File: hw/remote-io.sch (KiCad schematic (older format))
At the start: 0 parts

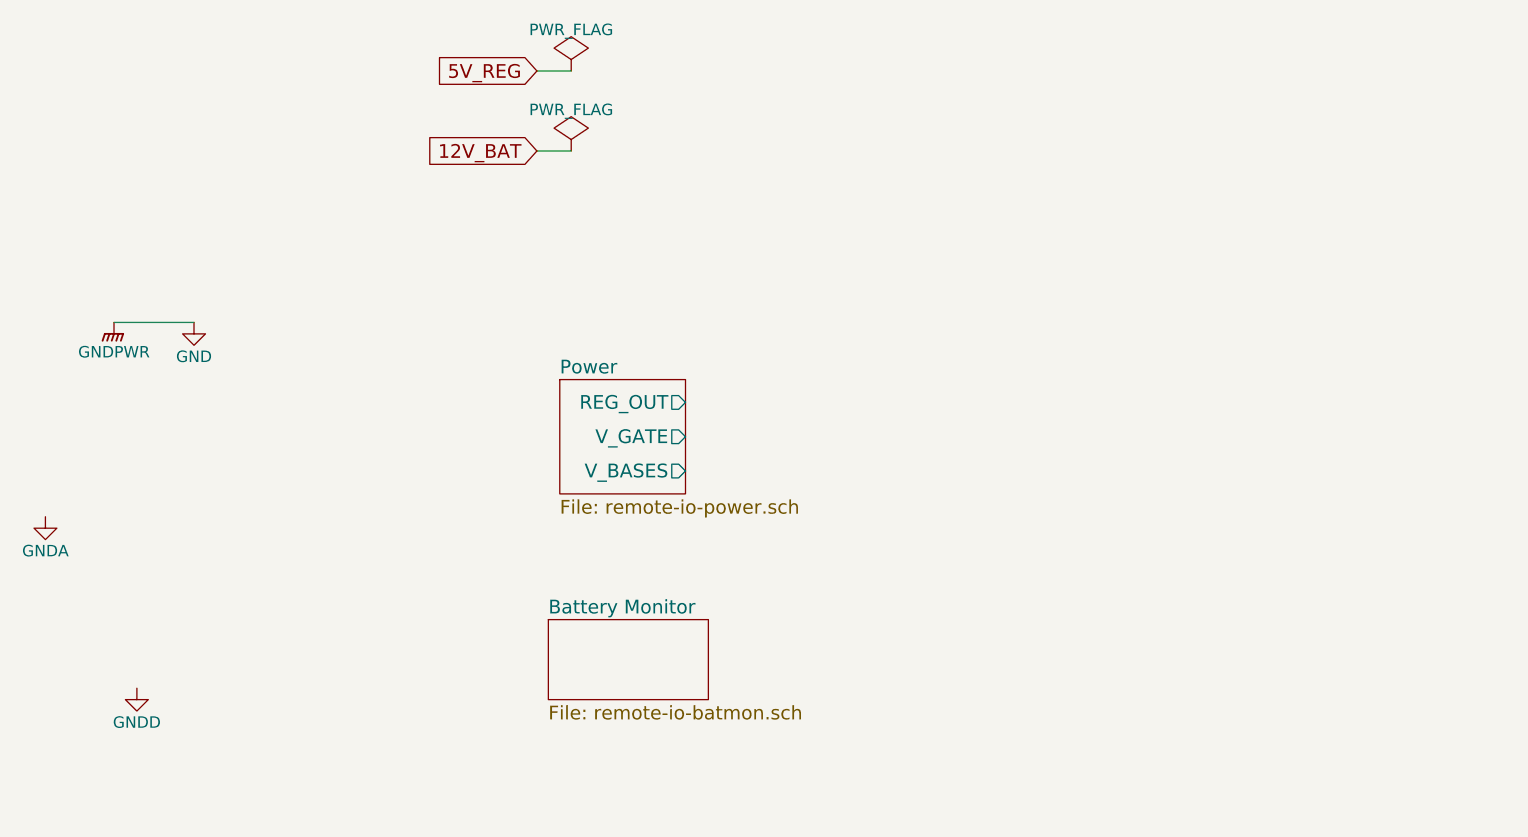
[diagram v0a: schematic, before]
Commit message: Added ADC schematic and connections
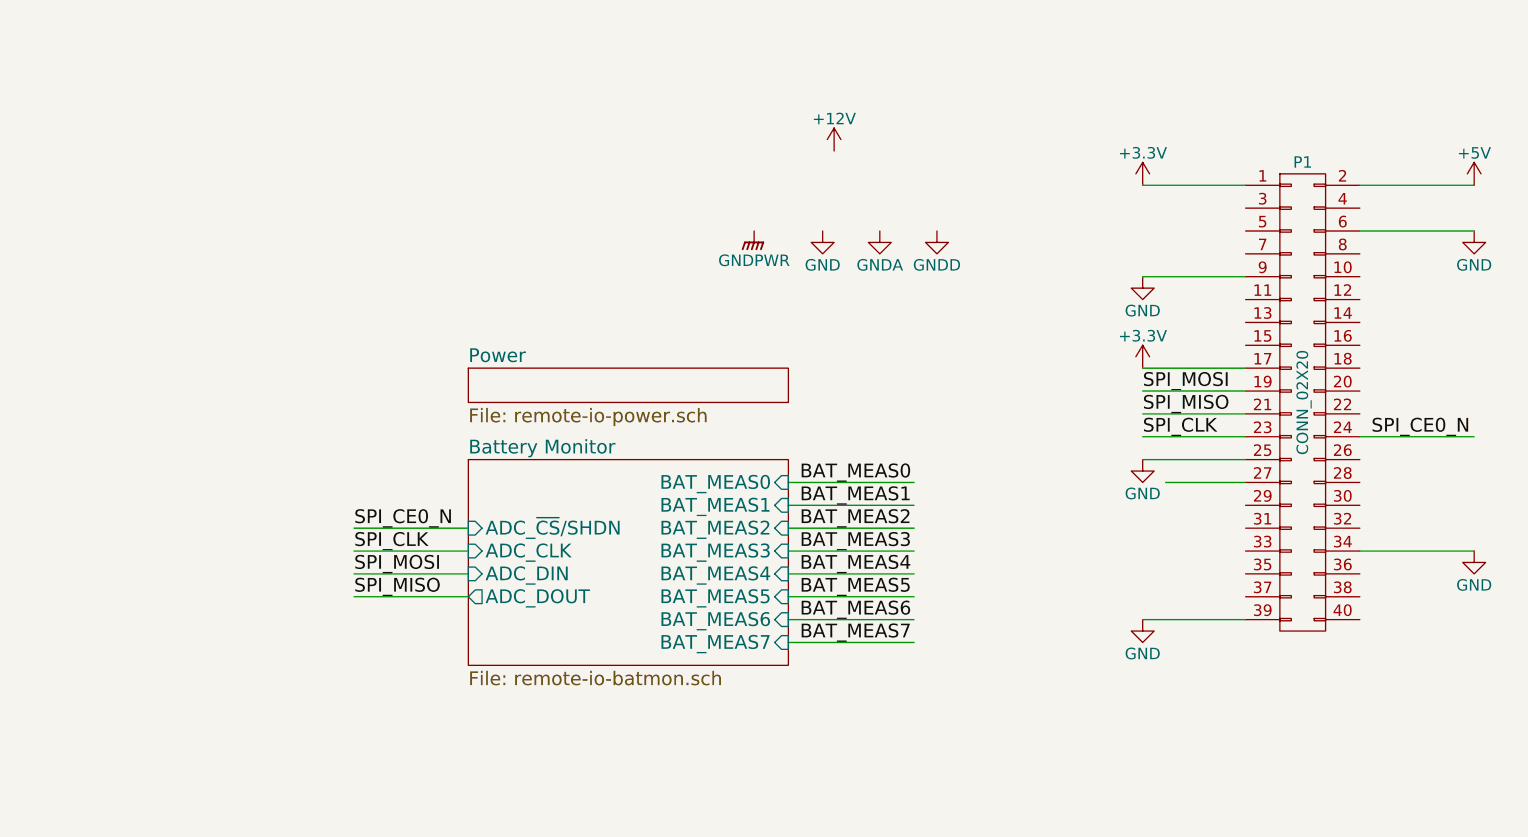
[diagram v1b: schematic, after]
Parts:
- added P1: CONN_02X20, symbol CONN_02X20
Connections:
- net labels added: +12V, +3.3V, +5V, BAT_MEAS0, BAT_MEAS1, BAT_MEAS2, BAT_MEAS3, BAT_MEAS4, BAT_MEAS5, BAT_MEAS6, BAT_MEAS7, SPI_CE0_N, SPI_CLK, SPI_MISO, SPI_MOSI
- net labels removed: 12V_BAT, 5V_REG
- wire segments 3 -> 25

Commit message: Added I2C ID EEPROM
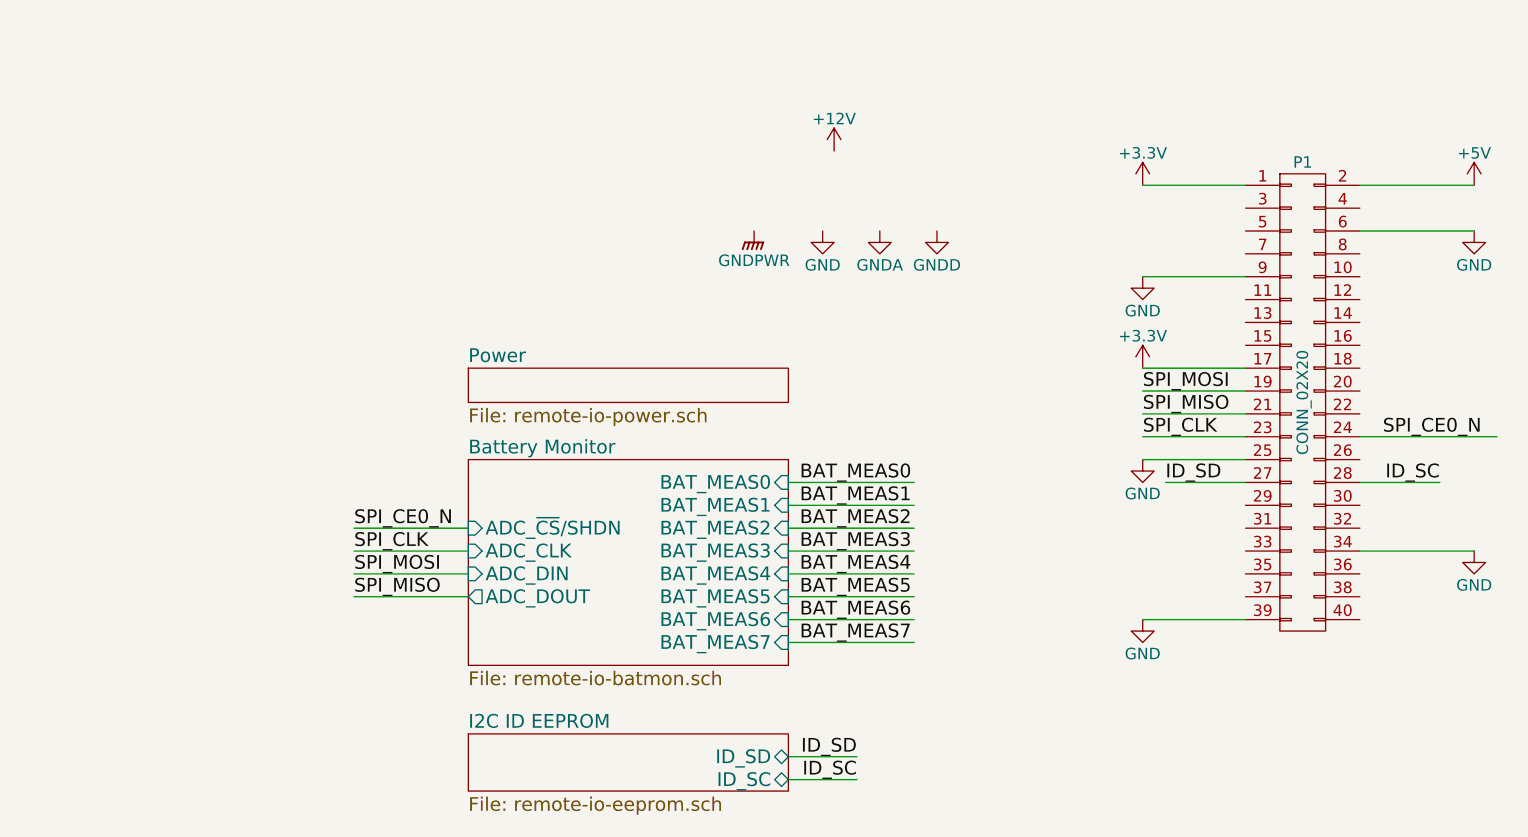
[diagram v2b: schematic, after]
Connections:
- net labels added: ID_SC, ID_SD
- wire segments 25 -> 28
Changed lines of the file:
@@
 $Descr USLetter 11000 8500
 encoding utf-8
-Sheet 1 3
+Sheet 1 4
 Title "Remote I/O Top Level"
 Date "2015-06-15"
@@
 Text Label 7050 2550 0    60   ~ 0
 SPI_MOSI
-Text Label 8050 2750 0    60   ~ 0
-SPI_CE0_N
 Text Label 7050 2750 0    60   ~ 0
 SPI_CLK
@@
 Wire Wire Line
 	7500 2550 7050 2550
-Wire Wire Line
-	8000 2750 8500 2750
 Wire Wire Line
 	7050 2750 7500 2750
@@
 Wire Wire Line
 	5500 3650 6050 3650
+Text Label 7150 2950 0    60   ~ 0
+ID_SD
+Wire Wire Line
+	8350 2950 8000 2950
+Text Label 8350 2950 2    60   ~ 0
+ID_SC
+$Sheet
+S 4100 4050 1400 250
+U 55817EDD
+F0 "I2C ID EEPROM" 60
+F1 "remote-io-eeprom.sch" 60
+F2 "ID_SC" B R 5500 4250 60
+F3 "ID_SD" B R 5500 4150 60
+$EndSheet
+Wire Wire Line
+	5800 4150 5500 4150
+Text Label 5800 4150 2    60   ~ 0
+ID_SD
+Wire Wire Line
+	5800 4250 5500 4250
+Text Label 5800 4250 2    60   ~ 0
+ID_SC
+Text Label 8100 2750 0    60   ~ 0
+SPI_CE0_N
+Wire Wire Line
+	8000 2750 8600 2750
 $EndSCHEMATC
